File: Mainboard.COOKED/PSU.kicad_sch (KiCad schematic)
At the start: 126 parts, among them J17 Barrel_Jack_Switch, J18 USB_C_Receptacle_USB2.0, J19 WAFER-MX1.25-10PCB, Q11 2N7002, Q12 2N7002, Q13 2N7002, Q14 2N7002, Q15 2N7002, Q16 AO3407, Q5 2N7002, Q6 2N7002, Q7 NCE30P28Q, Q8 2N7002, SW1 SW_Push, SW2 SW_Push, U13 TL431DBZ, U14 CH224K, U15 SY8253ADC, U16 SY8253ADC, U17 HM7533HBPR, U19 ULC0524P

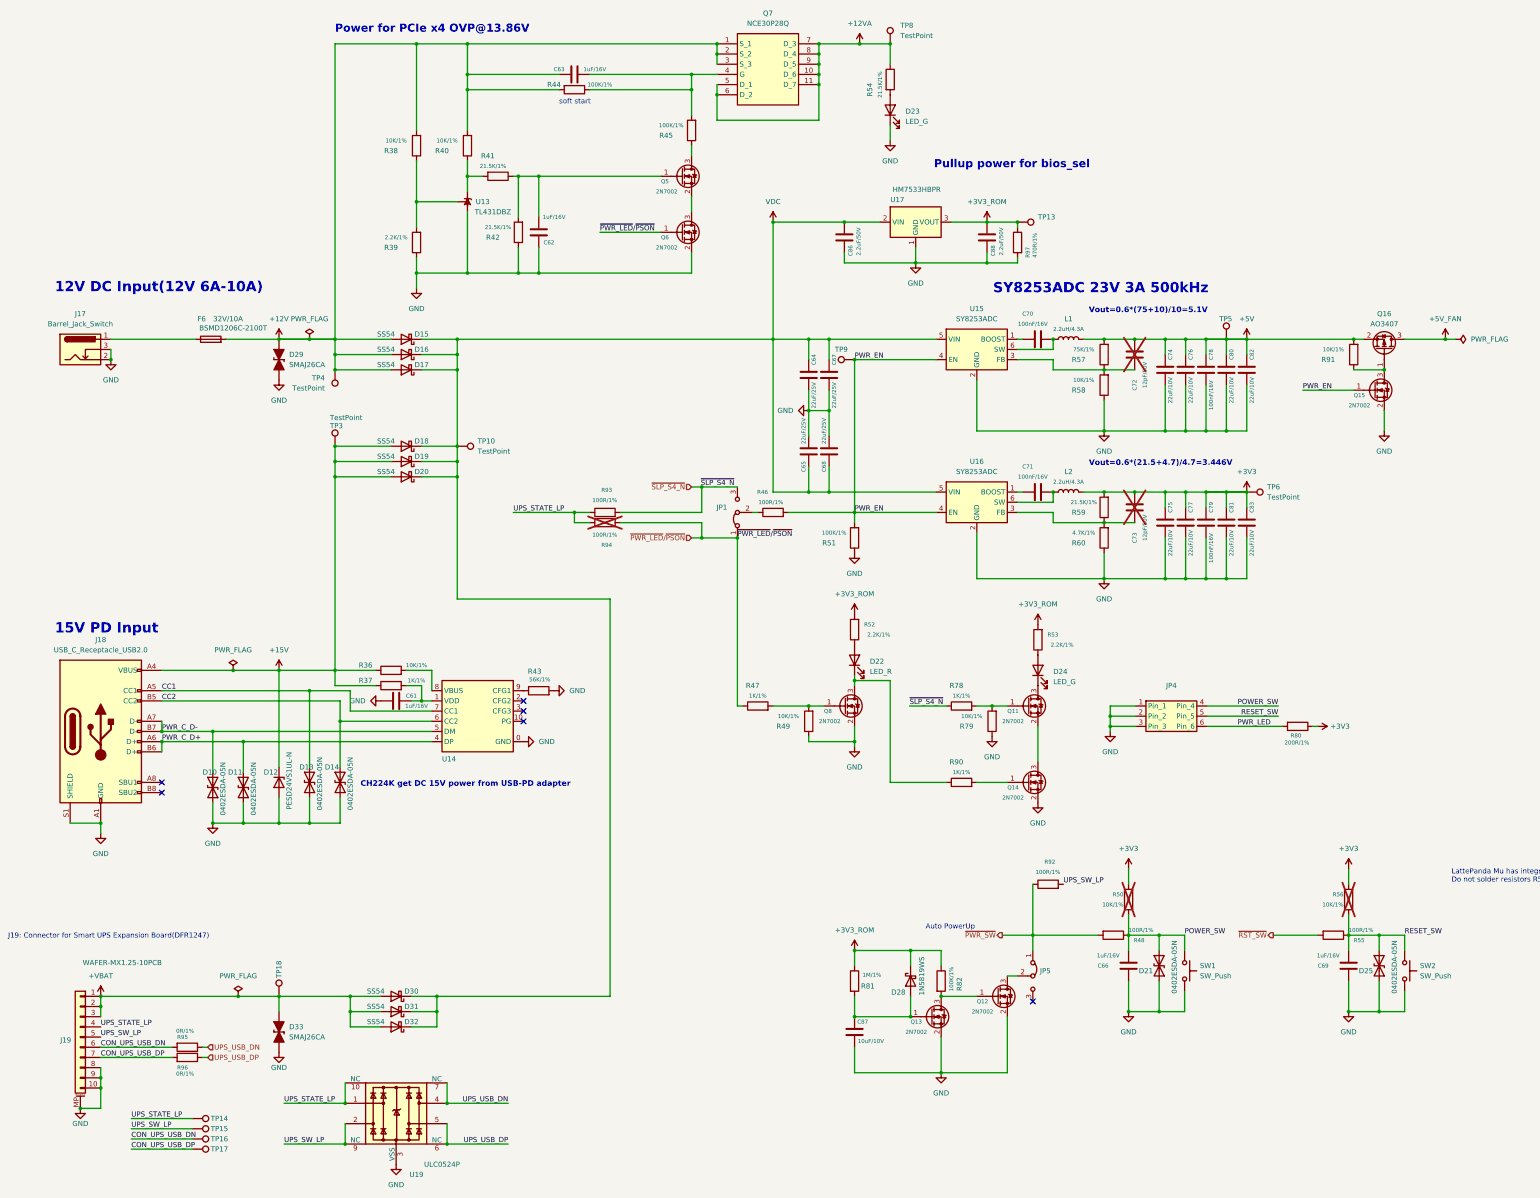
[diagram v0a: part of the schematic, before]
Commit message: "Scrapped" the current Mainboard, seems to be very broken for no reason.
It is being kept for now so that work done for the displays can be copied over later.
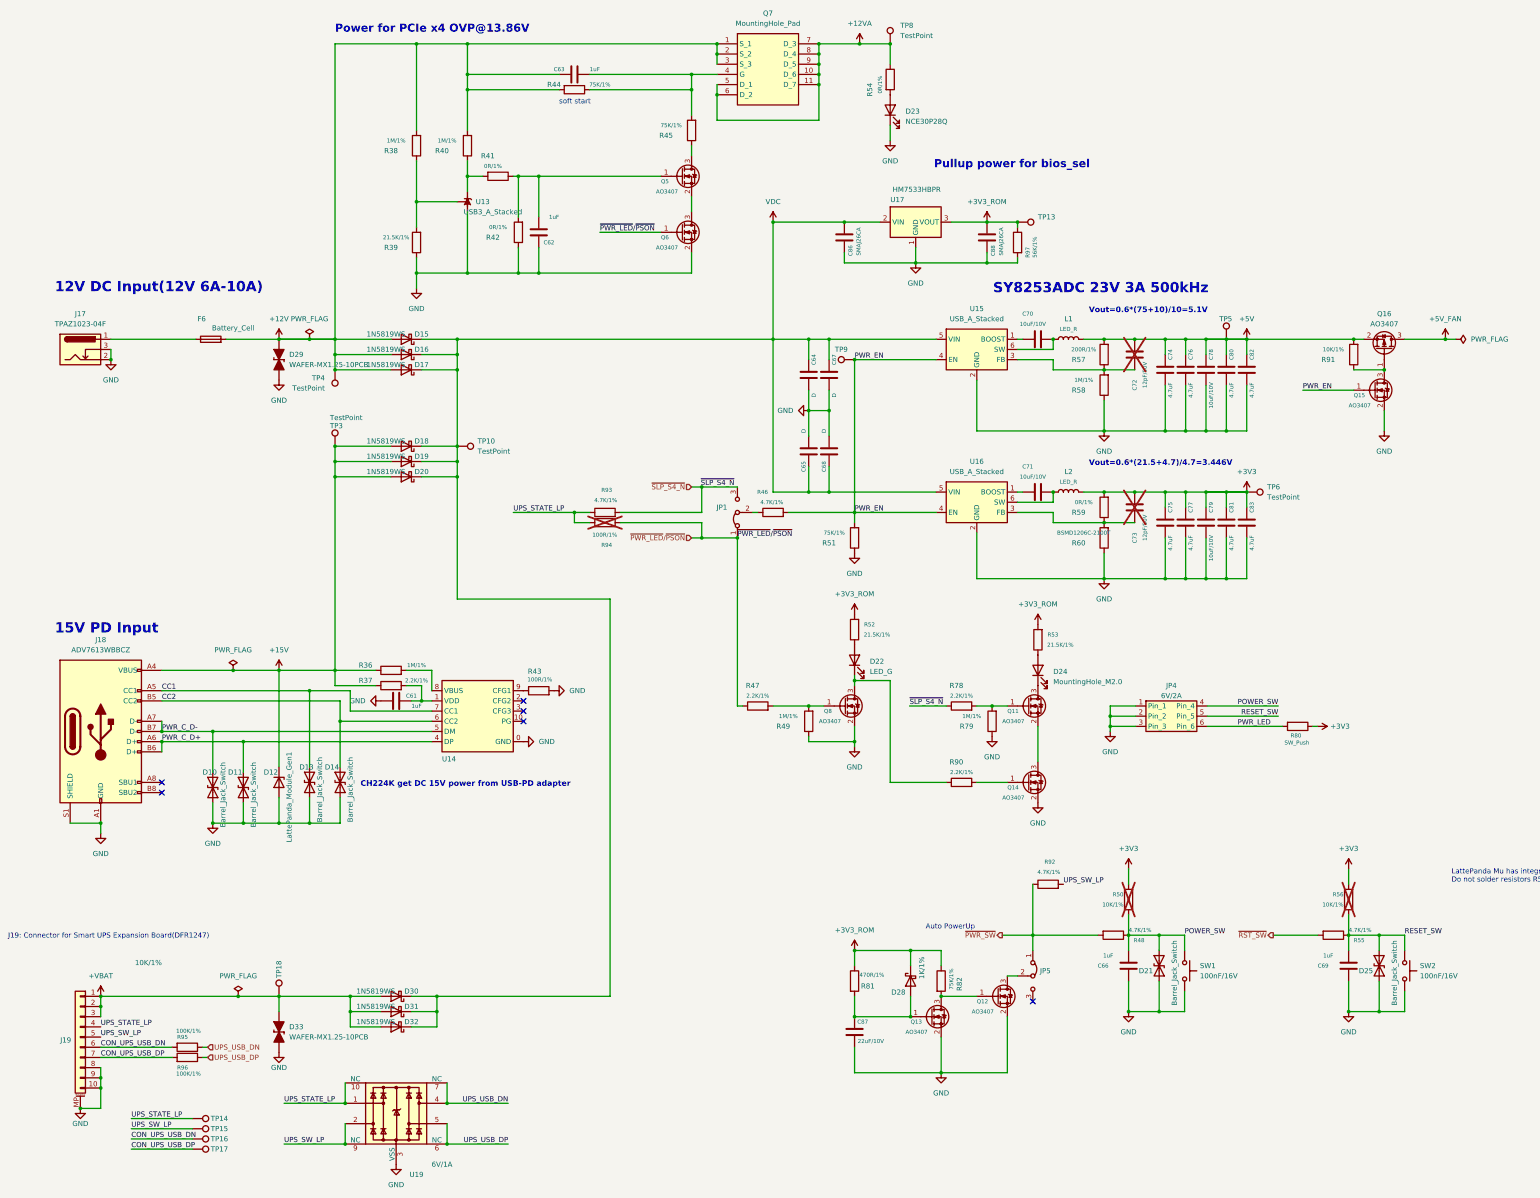
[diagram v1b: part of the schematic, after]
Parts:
- C61, C62, C63, C66, C69: value 1uF/16V -> 1uF; footprint A_HDJ_Library:C_0402_1005Metric -> A_HDJ_Library:C_0603_1608Metric; DF_Comment 贴片电容0402-1uF-16V-X5R(0402) -> 贴片电容0603-22uF-10V-X5R(0603); SCH_Show_Footprint C0402 -> C603
- C64, C65, C67, C68: value 22uF/25V -> D; footprint Capacitor_SMD:C_0805_2012Metric -> Diode_SMD:D_01005_0402Metric; DF_Comment 贴片电容0805-22uF-25V-X5R -> (none); SCH_Show_Footprint C603 -> (none)
- C70, C71, C78, C79: value 100nF/16V -> 10uF/10V; DF_Comment 贴片电容0402-100nF-16V-X7R(0402) -> 贴片电容0402-10UF-10V-X5R_GRM155R61A106ME44D; SCH_Show_Footprint C0402 -> -- mixed values --
- C74, C75, C76, C77, C80, C81, C82, C83: value 22uF/10V -> 4.7uF
- C86: value 2.2uF/50V -> SMAJ26CA; footprint A_DFRobot:C_0603 -> Diode_SMD:D_SMA; DF_Comment 贴片电容0603-2.2uF-50V-X5R -> 双向TVS管-SMAJ26CA-SMA
- C87: value 10uF/10V -> 22uF/10V; footprint A_HDJ_Library:C_0402_1005Metric -> A_HDJ_Library:C_0603_1608Metric; DF_Comment 贴片电容0402-10UF-10V-X5R_GRM155R61A106ME44D -> 贴片电容0603-22uF-10V-X5R(0603); SCH_Show_Footprint (none) -> C603
- C88: value 2.2uF/50V -> SMAJ26CA; footprint A_DFRobot:C_0603 -> Diode_SMD:D_SMA; DF_Comment 贴片电容0603-2.2uF-50V-X5R -> 双向TVS管-SMAJ26CA-SMA; SCH_Show_Footprint C0603 -> (none)
- D10, D11, D13, D14, D21, D25: value 0402ESDA-05N -> Barrel_Jack_Switch; footprint A_HDJ_Library:D_0402_1005Metric -> A_HDJ_Library:DC_Jack_DC007B_30V_10A; Buy_Link (none) -> https://item.szlcsc.com/19360929.html; DF_Comment 5.0V双向静电保护管_0402ESDA-05N -> DC2.5电源母座_12V/10A_XDJK-060B-055; SCH_Show_Footprint D0402 -> (none)
- D12: value PESD24VS1UL-N -> LattePanda_Module_Gen1; footprint A_HDJ_Library:D_0402_1005Metric -> A_HDJ_Library:DDR4_SODIMM_260P_8.0H_STD; Buy_Link https://item.szlcsc.com/393990.html -> https://item.szlcsc.com/5812308.html; DF_Comment 单向静电保护二极管_PESD24VS1UL-N_DFN1006 -> 连接器_DDR4-SODIMM-260P-8H_TE_2309411-1; SCH_Show_Footprint D0402 -> (none)
- D15, D16, D17, D18, D19, D20, D30, D31, D32: value SS54 -> 1N5819WS; footprint A_DFRobot:D_SMA -> Diode_SMD:D_SOD-323; DF_Comment 二极管-SS54-SMA(SMA) -> 二极管-1N5819W-SOD323备选型号:B5819WS、JSPD140A; SCH_Show_Footprint SMA -> -- mixed values --
- D22: value LED_R -> LED_G; DF_Comment 贴片LED红色0603(0603) -> 贴片LED绿色0603(1.8~2.4V,567~576nm)黄绿普亮
- D23: value LED_G -> NCE30P28Q; footprint A_HDJ_Library:LED_0603_1608Metric -> A_HDJ_Library:MOSFET_PDFN8_3.3x3.3; DF_Comment 贴片LED红色0603(0603) -> PMOS管NCE30P28Q-DFN3.3X3.3-8L; SCH_Show_Footprint LED0603 -> (none)
- D24: value LED_G -> MountingHole_M2.0; footprint A_HDJ_Library:LED_0603_1608Metric -> A_HDJ_Library:MountingHole_2.75mm_M2_4.4mm_Pad_TopOnly; Buy_Link (none) -> https://item.taobao.com/item.htm?abbucket=8&id=655855111684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; DF_Comment 贴片LED绿色0603(1.8~2.4V,567~576nm)黄绿普亮 -> 贴片螺母柱M2XC4X2.5+C2.7X1.5（无铅铜）; SCH_Show_Footprint LED0603 -> (none)
- D28: value 1N5819WS -> 1K/1%; footprint A_DFRobot:D_SOD-323 -> A_HDJ_Library:R_0402_1005Metric; DF_Comment 二极管-1N5819W-SOD323备选型号:B5819WS、JSPD140A -> 贴片电阻0402-1K-1%
- D29, D33: value SMAJ26CA -> WAFER-MX1.25-10PCB; footprint A_DFRobot:D_SMA -> A_DFRobot:MX1.25-10P-SMD; Buy_Link (none) -> https://item.szlcsc.com/3561406.html; DF_Comment 双向TVS管-SMAJ26CA-SMA -> WAFER-MX1.25-10PCB
- F6: value BSMD1206C-2100T -> Battery_Cell; footprint A_DFRobot:R_1206 -> A_HDJ_Library:Battery_Holder_CR1220_S8411-45R; Buy_Link https://item.szlcsc.com/43118985.html -> https://item.szlcsc.com/1049689.html; DF_Comment 一次性保险丝_BSMD1206C-2100T_32V-10A -> CR1220电池座贴片塑料
- J17: value Barrel_Jack_Switch -> TPAZ1023-04F; footprint A_HDJ_Library:DC_Jack_DC007B_30V_10A -> A_HDJ_Library:Diodes_UDFN-10_1.0x2.5mm_P0.5mm; Buy_Link https://item.szlcsc.com/19360929.html -> https://item.szlcsc.com/2973358.html; DF_Comment DC2.5电源母座_12V/10A_XDJK-060B-055 -> ESD静电保护IC-TPAZ1023-04F-DFN2510-10L
- J18: value USB_C_Receptacle_USB2.0 -> ADV7613WBBCZ; footprint A_HDJ_Library:USB_C_Receptacle_G-Switch_GT-USB-7010ASV -> BC_100_4_ADI; DF_Comment USB Type-C母座-U263-163N-4BS1735 5A -> (none)
- J19: value WAFER-MX1.25-10PCB -> 10K/1%; footprint A_DFRobot:MX1.25-10P-SMD -> A_HDJ_Library:R_0402_1005Metric; Buy_Link https://item.szlcsc.com/3561406.html -> (none); DF_Comment WAFER-MX1.25-10PCB -> 贴片电阻0402-10K-1%
- JP1: value Jumper_3_Bridged12 -> 2004850740; footprint A_HDJ_Library:PinHeader_1x03_P2.54mm_Vertical -> 200485-0740:CON_2004850740; DF_Comment 2.54黑色单排排针-3P -> (none)
- JP4: value (none) -> 6V/2A; footprint Connector_PinHeader_2.54mm:PinHeader_2x03_P2.54mm_Vertical -> Fuse:Fuse_0805_2012Metric; Buy_Link (none) -> https://item.szlcsc.com/947787.html; DF_Comment 2.54黑色3x2P排针 -> 0805贴片自恢复保险丝2A-6V_BSMD0805L-200; SCH_Show_Footprint (none) -> R0805
- JP5: value Jumper_3_Bridged12 -> 200485-0710; footprint A_DFRobot:PinHeader_1x03_P2.54mm_Vertical -> 200485-0710:2004850710; DF_Comment 2.54黑色单排排针-3P -> (none); Height (none) -> 5.7; Manufacturer_Name (none) -> Molex; Manufacturer_Part_Number (none) -> 200485-0710; Mouser Part Number (none) -> 538-200485-0710; Mouser Price/Stock (none) -> https://www.mouser.co.uk/ProductDetail/Molex/200485-0710?qs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
- L1, L2: value 2.2uH/4.3A -> LED_R; footprint A_HDJ_Library:L_Sunlord_SWPA4020S -> A_HDJ_Library:LED_0603_1608Metric; DF_Comment WPN4020H2R2MT 2.2UH 20% 额定电流4.3A 顺络 -> 贴片LED红色0603(0603); SCH_Show_Footprint (none) -> LED0603
- Q11, Q12, Q13, Q14, Q15, Q5, Q6, Q8: value 2N7002 -> AO3407; DF_Comment 2N7002-N沟道MOS管-SOT-23[备选型号:JMTL2N7002K] -> PMOS管AO3407-SOT23-3
- Q7: value NCE30P28Q -> MountingHole_Pad; footprint A_HDJ_Library:MOSFET_PDFN8_3.3x3.3 -> A_HDJ_Library:MountingHole_3mm_M2_Pad_TopOnly; Buy_Link (none) -> https://item.taobao.com/item.htm?abbucket=8&id=655855111684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; DF_Comment PMOS管NCE30P28Q-DFN3.3X3.3-8L -> 贴片螺母柱M2XC4X5.5+C3X1.5（无铅铜）
- R36, R38, R40, R49, R58, R79: value 10K/1% -> 1M/1%; footprint A_DFRobot:R_0402 -> A_HDJ_Library:R_0402_1005Metric; DF_Comment 贴片电阻0402-10K-1% -> 贴片电阻0402-1M-1%
- R37, R47, R78, R90: value 1K/1% -> 2.2K/1%; footprint A_DFRobot:R_0402 -> A_HDJ_Library:R_0402_1005Metric; DF_Comment 贴片电阻0402-1K-1% -> 贴片电阻0402-2.2K-1%
- R39, R52, R53: value 2.2K/1% -> 21.5K/1%; footprint A_DFRobot:R_0402 -> A_HDJ_Library:R_0402_1005Metric; DF_Comment 贴片电阻0402-2.2K-1% -> 贴片电阻0402-21.5K-1%
- R41, R42, R54, R59: value 21.5K/1% -> 0R/1%; footprint A_DFRobot:R_0402 -> A_HDJ_Library:R_0402_1005Metric; DF_Comment 贴片电阻0402-21.5K-1% -> 贴片电阻0402-0R-1%
- R43: value 56K/1% -> 100R/1%; footprint A_DFRobot:R_0402 -> A_HDJ_Library:R_0402_1005Metric; DF_Comment 贴片电阻0402-56K-1%(0402) -> 贴片电阻0402-100R-1%
- R44, R45, R51, R82: value 100K/1% -> 75K/1%; footprint A_DFRobot:R_0402 -> A_HDJ_Library:R_0402_1005Metric; DF_Comment 贴片电阻0402-100K-1% -> 贴片电阻0402-75K-1%
- R46, R48, R55, R92, R93: value 100R/1% -> 4.7K/1%; footprint A_DFRobot:R_0402 -> A_HDJ_Library:R_0402_1005Metric; DF_Comment 贴片电阻0402-100R-1% -> 贴片电阻0402-4.7K-1%
- R57: value 75K/1% -> 200R/1%; footprint A_DFRobot:R_0402 -> A_HDJ_Library:R_0402_1005Metric; DF_Comment 贴片电阻0402-75K-1% -> 贴片电阻0402-200R-1%
- R60: value 4.7K/1% -> BSMD1206C-2100T; footprint A_DFRobot:R_0402 -> Resistor_SMD:R_1206_3216Metric; Buy_Link (none) -> https://item.szlcsc.com/43118985.html; DF_Comment 贴片电阻0402-4.7K-1% -> 一次性保险丝_BSMD1206C-2100T_32V-10A
- R80: value 200R/1% -> SW_Push; footprint A_DFRobot:R_0402 -> A_DFRobot:SW_PUSH_SIDE_TS-1012EV_7.7x3.95x3.5mm; DF_Comment 贴片电阻0402-200R-1% -> 侧按卧插4脚开关-TS-1012EV-26-7*3.5*3.5
- R81: value 1M/1% -> 470R/1%; footprint A_DFRobot:R_0402 -> A_HDJ_Library:R_0402_1005Metric; DF_Comment 贴片电阻0402-1M-1% -> 贴片电阻0402-470R-1%
- R95, R96: value 0R/1% -> 100K/1%; footprint A_DFRobot:R_0402 -> A_HDJ_Library:R_0402_1005Metric; DF_Comment 贴片电阻0402-0R-1% -> 贴片电阻0402-100K-1%
- R97: value 470R/1% -> 56K/1%; footprint A_DFRobot:R_0402 -> A_HDJ_Library:R_0402_1005Metric; DF_Comment 贴片电阻0402-470R-1% -> 贴片电阻0402-56K-1%(0402)
- SW1, SW2: value SW_Push -> 100nF/16V; footprint A_DFRobot:SW_PUSH_SIDE_TS-1012EV_7.7x3.95x3.5mm -> A_HDJ_Library:C_0402_1005Metric; DF_Comment 侧按卧插4脚开关-TS-1012EV-26-7*3.5*3.5 -> 贴片电容0402-100nF-16V-X7R(0402); SCH_Show_Footprint (none) -> C0402
- U13: value TL431DBZ -> USB3_A_Stacked; footprint A_HDJ_Library:SOT-23 -> A_HDJ_Library:USB3_A_Molex_48406-0001_Horizontal_Stacked; Buy_Link (none) -> https://item.szlcsc.com/3132965.html; DF_Comment 参考电压-TL431ACDBZR-SOT23（丝印TAC） -> 双层USB3.0_A母座_USB-303WSD-BRY
- U14: value CH224K -> Fan_4pin; footprint A_HDJ_Library:ESSOP-10-1EP_3.9x5mm_P1.0mm_EP3.2x2.3 -> A_HDJ_Library:JST_PH_B4B-PH-K_1x04_P2.00mm_Vertical; Buy_Link (none) -> https://item.szlcsc.com/255571.html; DF_Comment USB PD等快充协议受电芯片-CH224K-ESSOP10 -> PH2.0-4A直针插座(2.0-4P直)-DL
- U15, U16: value SY8253ADC -> USB_A_Stacked; footprint A_HDJ_Library:TSOT-23-6 -> A_HDJ_Library:USB_A_CUI_UJ2-ADH-TH_Horizontal_Stacked; Buy_Link https://item.szlcsc.com/94934.html -> (none); DF_Comment DCDC同步降压芯片_SY8253ADC_TSOT23-6 -> USB2.0-A型双层白胶母座
- U19: value ULC0524P -> 6V/1A; footprint A_HDJ_Library:Diodes_UDFN-10_1.0x2.5mm_P0.5mm -> A_HDJ_Library:Fuse_0805_2012Metric; Buy_Link (none) -> https://item.szlcsc.com/947770.html; DF_Comment ESD静电保护IC-BV-ULC0524P-DFN2510-10L -> 0805贴片自恢复保险丝1A-6V_BSMD0805-100-6V; SCH_Show_Footprint (none) -> R0603
